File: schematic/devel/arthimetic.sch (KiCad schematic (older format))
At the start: 29 parts

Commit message: separated symbol library according to functionality
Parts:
- U? (x2): symbol common:AD538 -> Analog_CU:AD538
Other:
- moved on the sheet: U?
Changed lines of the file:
@@
 LINEAR ARTHIMETIC
 $Comp
-L common:AD538 U?
+L Analog_CU:AD538 U?
 U 1 1 5D8D4EFB
 P 5400 1700
@@
 $EndComp
 $Comp
-L common:AD538 U?
+L Analog_CU:AD538 U?
 U 1 1 5D8D4F3C
 P 8250 1700

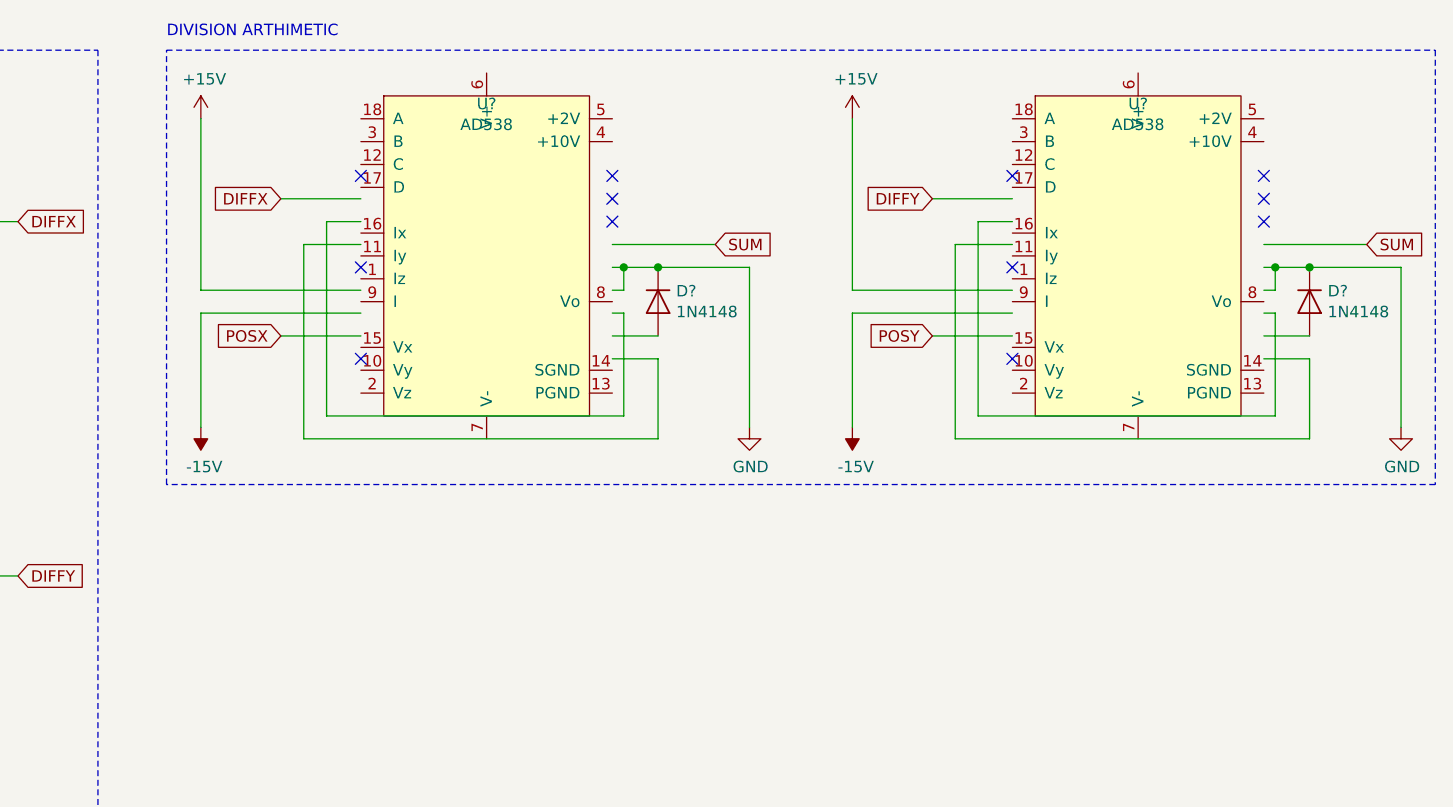
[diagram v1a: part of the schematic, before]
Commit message: redesigned AD538 symbol according to guidelines
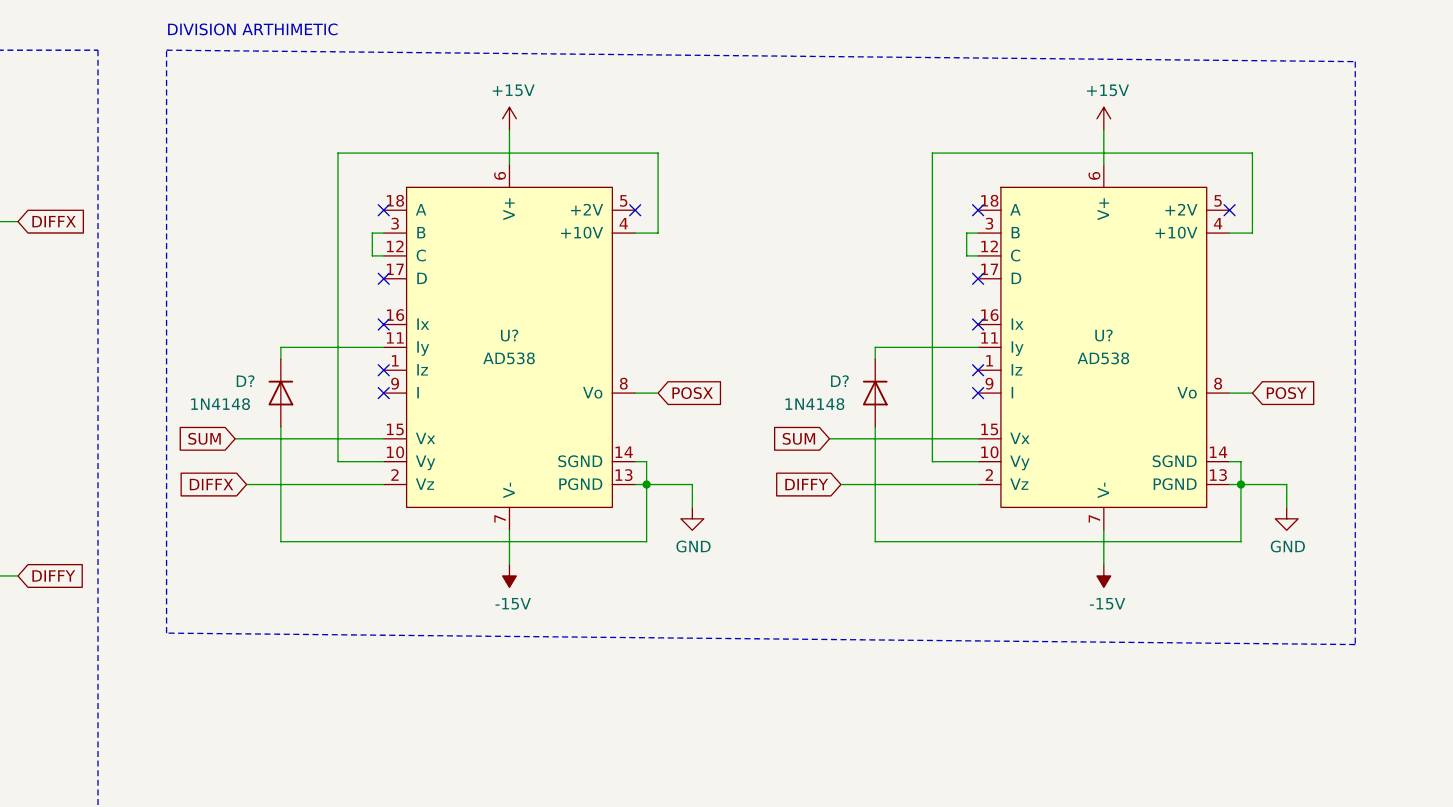
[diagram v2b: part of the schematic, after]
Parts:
- removed D?: 1N4148, Diode_THT:D_DO-35_SOD27_P7.62mm_Horizontal, symbol Diode:1N4148
- removed U?: AD538, symbol Analog_CU:AD538
- added D?: 1N4148, Diode_THT:D_DO-35_SOD27_P7.62mm_Horizontal, symbol Diode:1N4148
- added U?: AD538, symbol Analog_CU:AD538
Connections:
- wire segments 126 -> 124
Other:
- moved on the sheet: D?, U?

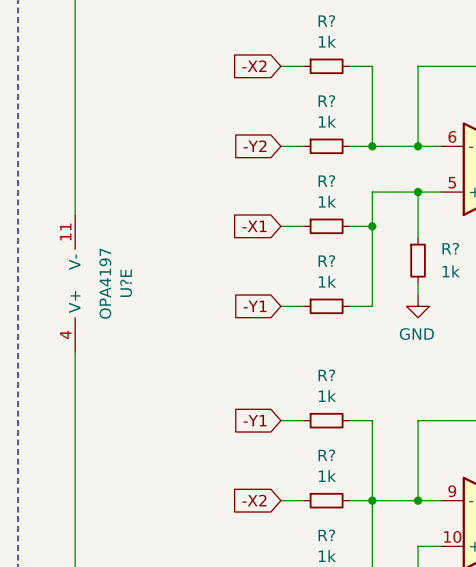
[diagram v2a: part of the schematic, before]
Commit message: fixed opamp supply voltage polarisation, fixed output buffers
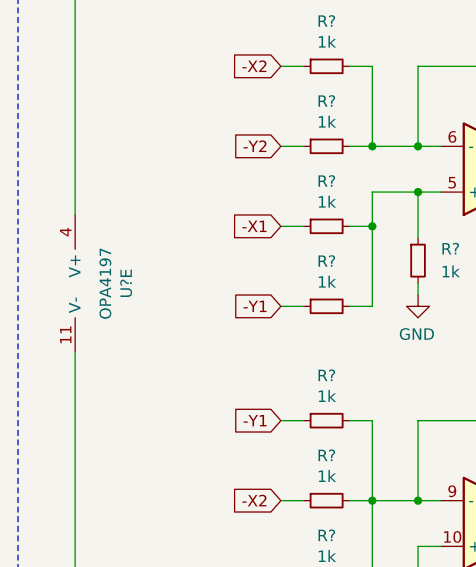
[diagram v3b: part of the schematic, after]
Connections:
- net +12V: now also U?.4 (V+); no longer U?.11 (V-)
- net -12V: now also U?.11 (V-); no longer U?.4 (V+)
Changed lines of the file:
@@
 F 3 "~" H 850 3600 50  0001 C CNN
 	5    850  3600
-	-1   0    0    1
+	-1   0    0    -1
 $EndComp
 Wire Wire Line

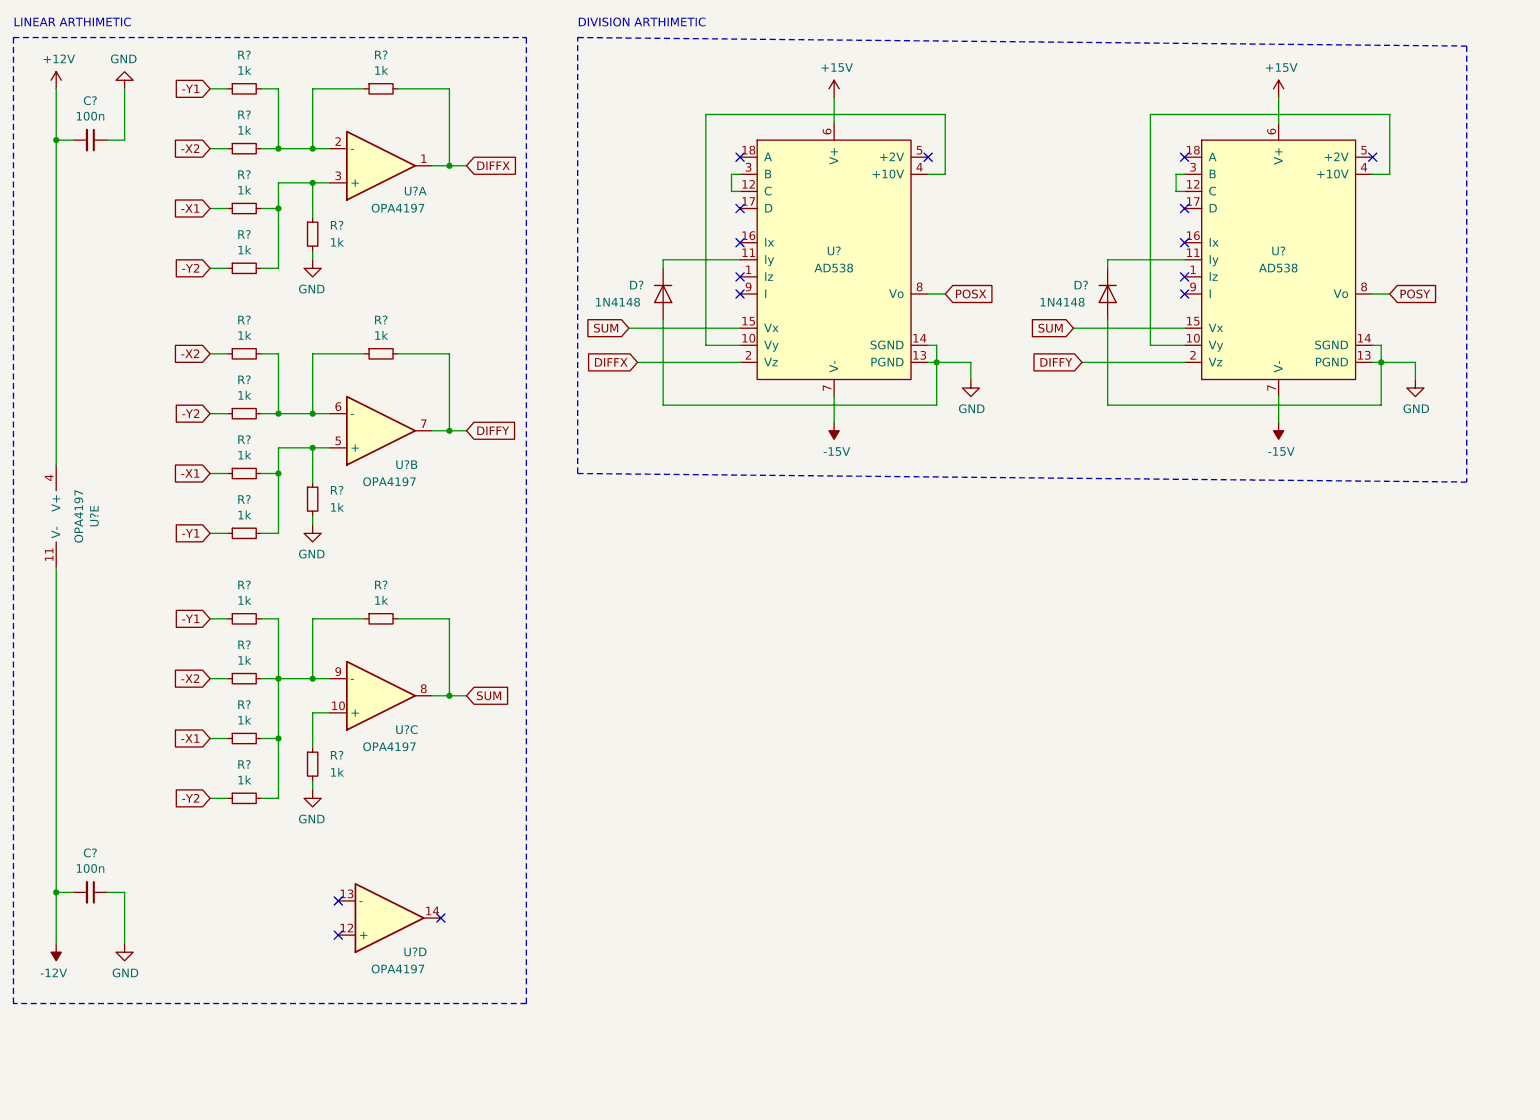
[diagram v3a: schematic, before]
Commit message: fixed floating buffer in arthimetic unit
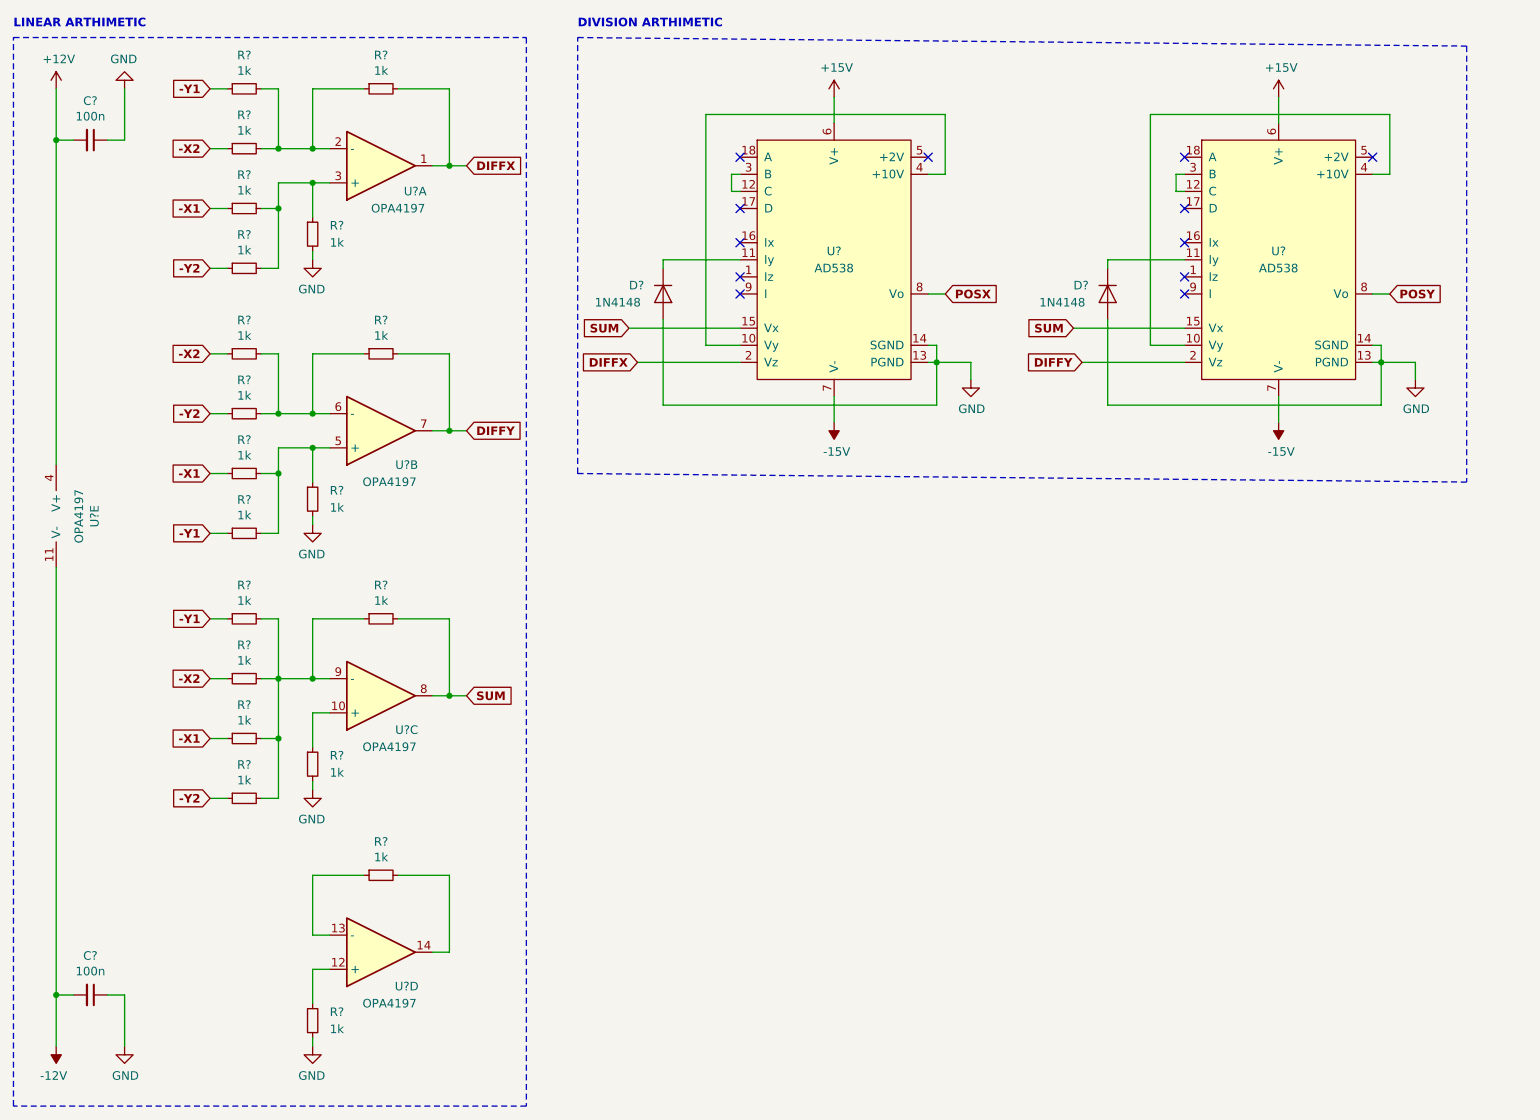
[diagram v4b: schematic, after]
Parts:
- removed U?: OPA4197, symbol Device:Opamp_Quad_Generic
- added R? (x2): 1k, symbol Device:R_Small
- added U?: OPA4197, symbol Device:Opamp_Quad_Generic
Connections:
- net GND: now also R?.2
- new net: R?.1, U?.12 (+)
- new net: R?.1, U?.13 (-)
- new net: R?.2, U?.14
- no-connect marks 15 -> 12
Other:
- moved on the sheet: C?
